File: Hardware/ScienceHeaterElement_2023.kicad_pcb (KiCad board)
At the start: 2 copper layers, 61.3 x 44.1 mm, 16 parts, among them Q1 BUK7M6R3-40EX, U1 LMT85DCK

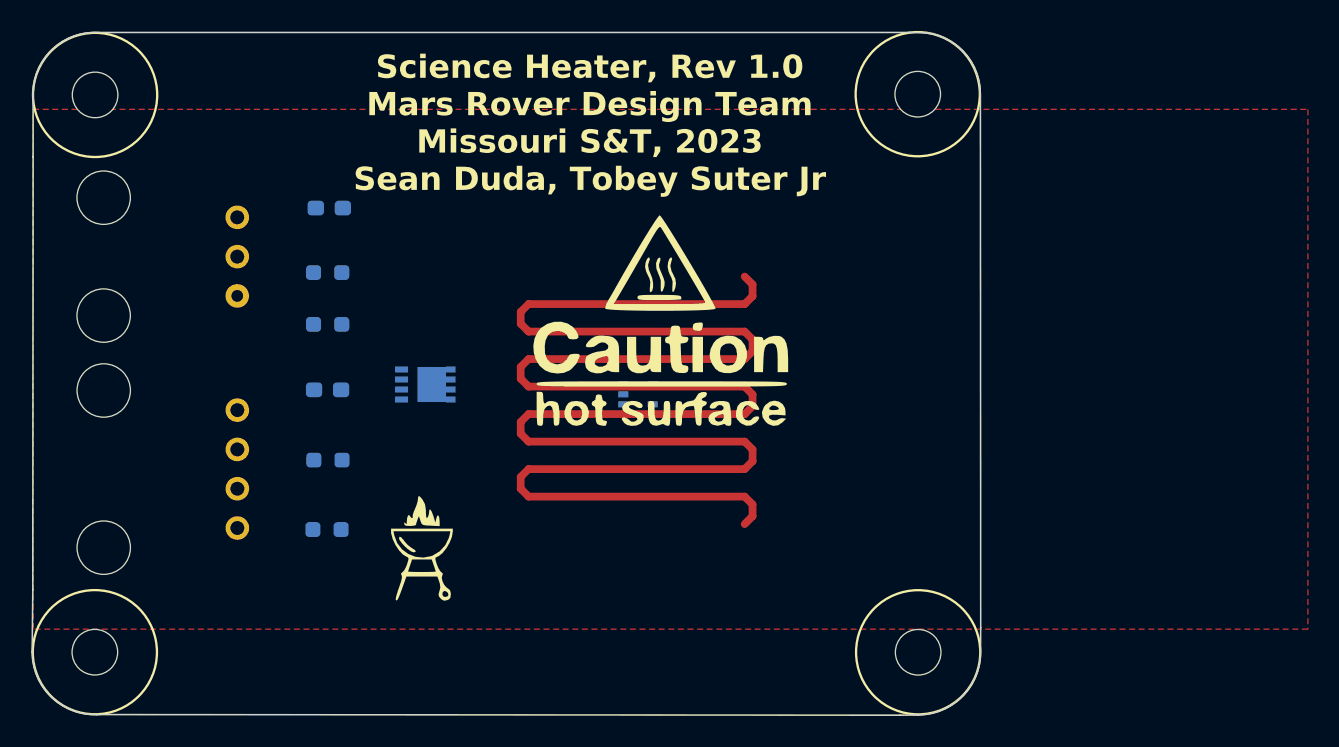
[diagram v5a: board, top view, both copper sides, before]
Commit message: Completed Changes
Completed final changes such as trace work, flipped components, changed gnd keep out
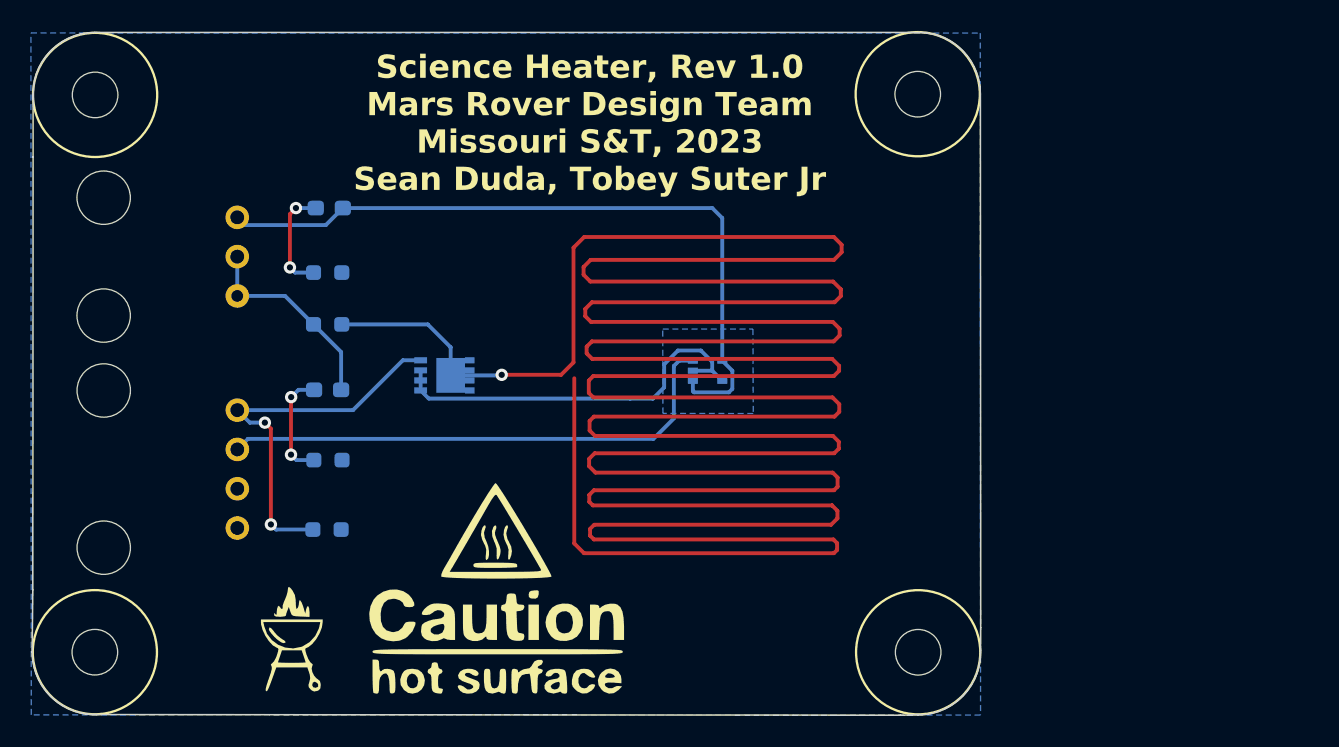
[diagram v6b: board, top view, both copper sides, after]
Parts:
- moved G*** 20.3 mm to (100.9, 68.1)
- moved G*** 10.3 mm to (87.7, 71.2)
- moved U1 4.75 mm to (114.6, 54.1)
- moved Q1 1.36 mm to (97.6, 54.4)
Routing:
- net /Heater_Trace: track 131.5 -> 343.9 mm, vias 0 -> 1
- net +3.3V: track 0.00 -> 47.0 mm
- net Temp_Sense: track 0.00 -> 33.8 mm
- net GND: track 0.00 -> 25.6 mm
- net Gate_Driving_Pin: track 0.00 -> 24.9 mm, vias 0 -> 2
- net +12V: track 0.00 -> 13.2 mm
- net Net-(D2-K): track 0.00 -> 7.02 mm, vias 0 -> 2
- net Net-(D1-K): track 0.00 -> 6.94 mm, vias 0 -> 2
- added copper zone on B.Cu, net /Heater_Trace
- added copper zone on B.Cu, net GND
- removed copper zone on F.Cu, net GND

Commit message: Updated layout for order
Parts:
- removed D2: Green, LED_SMD:LED_0603_1608Metric_Pad1.05x0.95mm_HandSolder
- removed R4: 4.7k, Resistor_SMD:R_0603_1608Metric_Pad0.98x0.95mm_HandSolder
- removed REF** (x4): 4_40_Hole, MRDT_Drill_Holes:4_40_Hole_Corner
- added G***: LOGO, LOGO, B.Cu at (105.2, 61.5)
- added G***: LOGO, LOGO, B.Cu at (91.9, 58.4)
- D1: value Green -> ORANGE
- Q1: value BUK7M6R3-40EX -> Si4162DY; footprint Package_TO_SOT_SMD:LFPAK33 -> Package_SO:SOIC-8_3.9x4.9mm_P1.27mm
- R1: value 2 -> 7.5; footprint Resistor_SMD:R_0603_1608Metric_Pad0.98x0.95mm_HandSolder -> Package_TO_SOT_THT:TO-126-2_Horizontal_TabDown
- R2: value 300 -> 1000
- R3: value 1k -> 4.7k
- moved R3 27.3 mm to (77.2, 35.8), turned to 180 degrees
- moved Q1 22.6 mm to (78.7, 41.9), turned to -90 degrees
- moved U1 20.2 mm to (94.7, 50.8), turned to 180 degrees
- moved D1 19.2 mm to (71.9, 49.5), turned to -90 degrees
- moved R2 15.5 mm to (74.7, 49.5), turned to 90 degrees
- moved R1 15.1 mm to (75.2, 53.9)
- moved Conn1 14.7 mm to (70.4, 39.4)
- moved Conn2 14.0 mm to (70.4, 54.6)
- moved G*** 10.00 mm to (98.6, 58.4)
- moved G*** 10.00 mm to (85.3, 61.5)
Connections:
- Conn1 pad 2: +12V -> Gate_Driving_Pin
- Conn1 pad 3: +12V -> Temp_Sense
- Conn2 pad 1: Gate_Driving_Pin -> +12V
- Conn2 pad 2: Temp_Sense -> +12V
- D1 pad 1: Net-(D1-K) -> /Heater_Trace
- D1 pad 2: +3.3V -> Net-(D1-A)
- R2 pad 1: Net-(D1-K) -> +12V
- R2 pad 2: GND -> Net-(D1-A)
- R3 pad 1: Net-(D2-K) -> Gate_Driving_Pin
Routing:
- net /Heater_Trace: track 343.9 -> 657.8 mm, vias 1 -> 7
- net +3.3V: track 47.0 -> 32.4 mm
- net GND: track 25.6 -> 18.1 mm, vias 0 -> 3
- net Net-(D2-K): track 7.02 -> 0.00 mm, vias 2 -> 0
- net Net-(D1-K): track 6.94 -> 0.00 mm, vias 2 -> 0
- net Gate_Driving_Pin: track 24.9 -> 19.0 mm, vias 2 -> 0
- net Temp_Sense: track 33.8 -> 28.6 mm
- net Net-(D1-A): track 0.00 -> 3.53 mm
- added copper zone on F.Cu, net GND
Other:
- board size 61.3 x 44.1 mm -> 50.8 x 38.1 mm

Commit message: Generated Gerbs
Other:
- board text added: "Science Heater, Rev 1.0 Mars Rover Design Team Missouri S&T, 2024 Sean Duda, Tobey Suter Jr"
- board text removed: "Science Heater, Rev 1.0 Mars Rover Design Team Missouri S&T, 2023 Sean Duda, Tobey Suter Jr"
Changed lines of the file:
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@@
       (outputformat 1)
       (mirror false)
-      (drillshape 1)
+      (drillshape 0)
       (scaleselection 1)
-      (outputdirectory "")
+      (outputdirectory "Gerbs/")
     )
   )
@@
   (gr_line (start 103.910001 69.85) (end 61.311781 69.85)
     (stroke (width 0.1) (type default)) (layer "Edge.Cuts"))
-  (gr_text "Science Heater, Rev 1.0\nMars Rover Design Team\nMissouri S&T, 2023\nSean Duda, Tobey Suter Jr" (at 88.9 42.672) (layer "F.SilkS")
+  (gr_text "Science Heater, Rev 1.0\nMars Rover Design Team\nMissouri S&T, 2024\nSean Duda, Tobey Suter Jr" (at 89.916 42.672) (layer "F.SilkS")
     (effects (font (size 1.5 1.5) (thickness 0.3) bold) (justify bottom))
   )
